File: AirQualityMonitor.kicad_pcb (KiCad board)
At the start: 4 copper layers, 72.3 x 62 mm, 177 parts, among them J1 USB_C_Receptacle_USB2.0_16P, J10 FH34SRJ-24S-0.5SH_99_E2417KS0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, J2 TC2050, J3 SM05B-GHS-TB, J4 Header, J5 BM02B-ACHSS-GAN-ETF, J6 SM04B-GHS-TB, J7 SM04B-GHS-TB, J8 SM06B-GHS-TB, J9 SM06B-GHS-TB, Q1 RV2C010UNT2L, Q2 RUM001L02T2CL, Q3 Si1308EDL, U1 TLV70033DDCR, U10 SGP41-D-R4, U11 PCA9306D, U12 SRV05-4, U13 BME690, U14 TXU0104PWR, U15 SN74LXC1T45DCKR, U16 TCK107AF,LF, U2 TLV70036DDCR, U3 USBLC6-2SC6, U4 TPS2553DDBVR, U5 nRF5340-QKxx, U6 MX25R3235FM1IH0-TR, U7 TCK107AF,LF, U8 NRF7001-QFAA-R, U9 BGS12WN6E6327, Y1 32M, Y2 32k768, Y3 Crystal_GND24

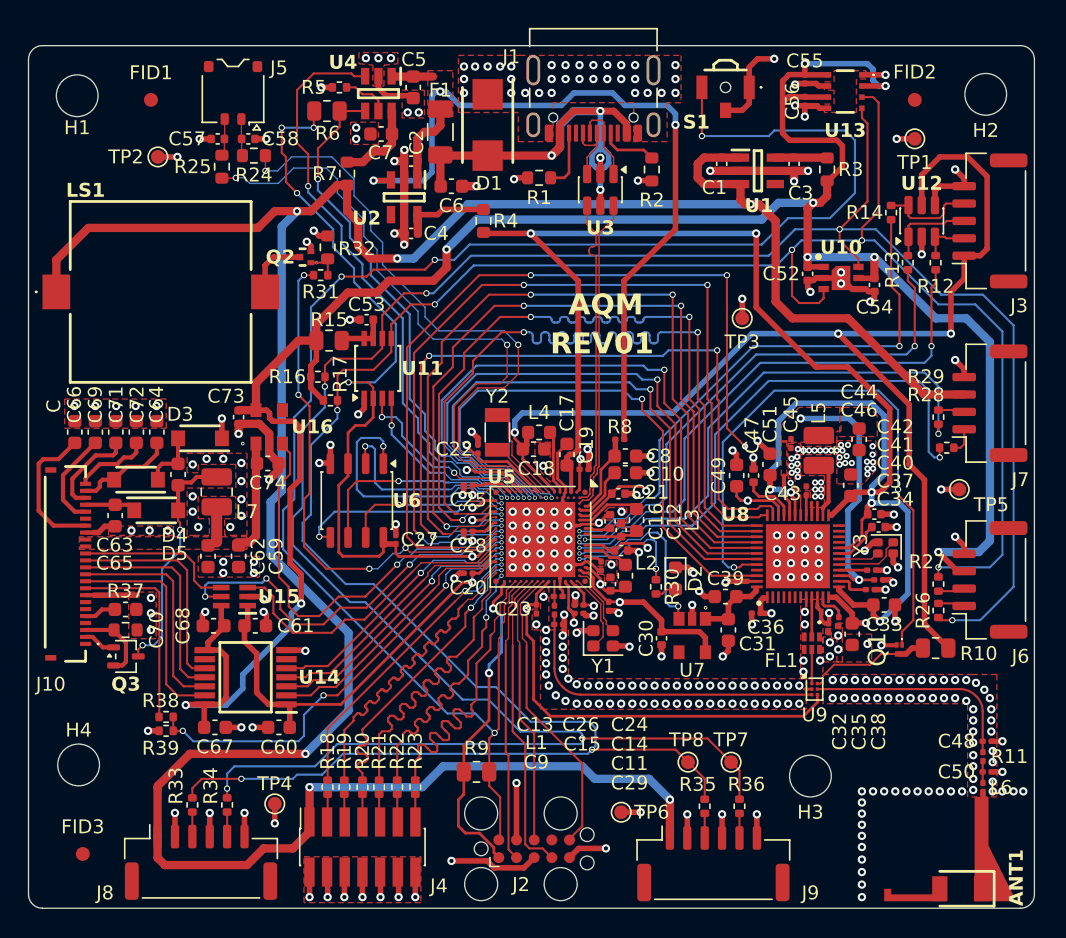
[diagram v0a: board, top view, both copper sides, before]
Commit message: Add project symbols and footprints
Move all self-made symbols and footprints to the lib folder.
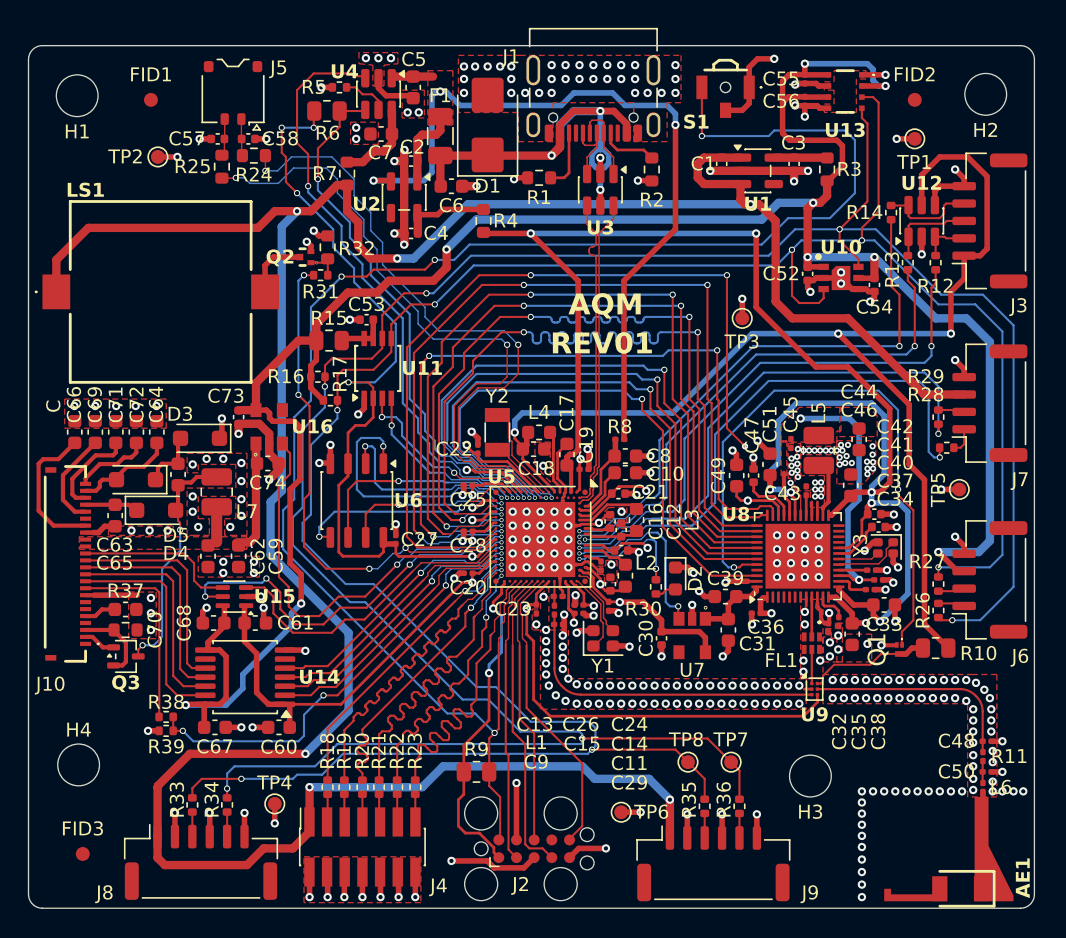
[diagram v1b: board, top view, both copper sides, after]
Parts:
- D1: footprint SMBJ5.0A:DIOM5436X244N -> Diode_SMD:D_SMB
- D3, D4, D5: footprint SS2040FL_R1_00001:SODFL3618X110N -> Diode_SMD:D_SOD-123F
- F1: footprint MyLib:Fuse_SF-1206F -> Fuse:Fuse_1206_3216Metric
- J5: footprint Connector_JST:JST_ACH_BM02B-ACHSS-GAN-ETF_1x02-1MP_P1.20mm_Vertical -> BM02B-ACHSS-GAN-ETF:JST_ACH_BM02B-ACHSS-GAN-ETF_1x02-1MP_P1.20mm_Vertical
- Q1: footprint RV2C010UNT2L:RV2C010UNT2L -> RV2C010UNT2L-Small:RV2C010UNT2L
- U1: footprint TLV70033DDCR:SOT95P280X110-5N -> Package_TO_SOT_SMD:SOT-23-5
- U14: footprint TXU0104PWR:SOP65P640X120-14N -> Package_SO:TSSOP-14_4.4x5mm_P0.65mm
- U15: footprint SN74LXC1T45DCKR:SOT65P210X110-6N -> Package_TO_SOT_SMD:SOT-363_SC-70-6
- U2: footprint TLV70036DDCR:SOT95P280X110-5N -> Package_TO_SOT_SMD:SOT-23-5
- U4: footprint TPS2553DDBVR:SOT95P280X145-6N -> Package_TO_SOT_SMD:SOT-23-6
- U5: footprint MyLib:Nordic_AQFN-94-1EP_7x7mm_P0.4mm -> nRF5340-QKxx:Nordic_AQFN-94-1EP_7x7mm_P0.4mm
- U8: footprint NRF7001-QFAA-R:QFN40P600X600X90-49N -> Package_DFN_QFN:QFN-48-1EP_6x6mm_P0.4mm_EP4.66x4.66mm
- U9: footprint MyLib:Infineon_PG-TSNP-6-10_0.7x1.1mm_0.7x1.1mm_P0.4mm -> BGS12WN6E6327:Infineon_PG-TSNP-6-10_0.7x1.1mm_0.7x1.1mm_P0.4mm
- moved F1 0.29 mm to (129.6, 44.5)
- moved C61 0.20 mm to (116.3, 79.5)
- moved C68 0.20 mm to (113.3, 79.5)
- turned D1 to 90 degrees
- renumbered ANT1 to AE1
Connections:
- D1 pad 1: GND -> +Vbus
- D1 pad 2: +Vbus -> GND
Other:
- board text added: "REV${REVISION}"
- board text removed: "REV01"
